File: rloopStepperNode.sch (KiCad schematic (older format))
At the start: 0 parts

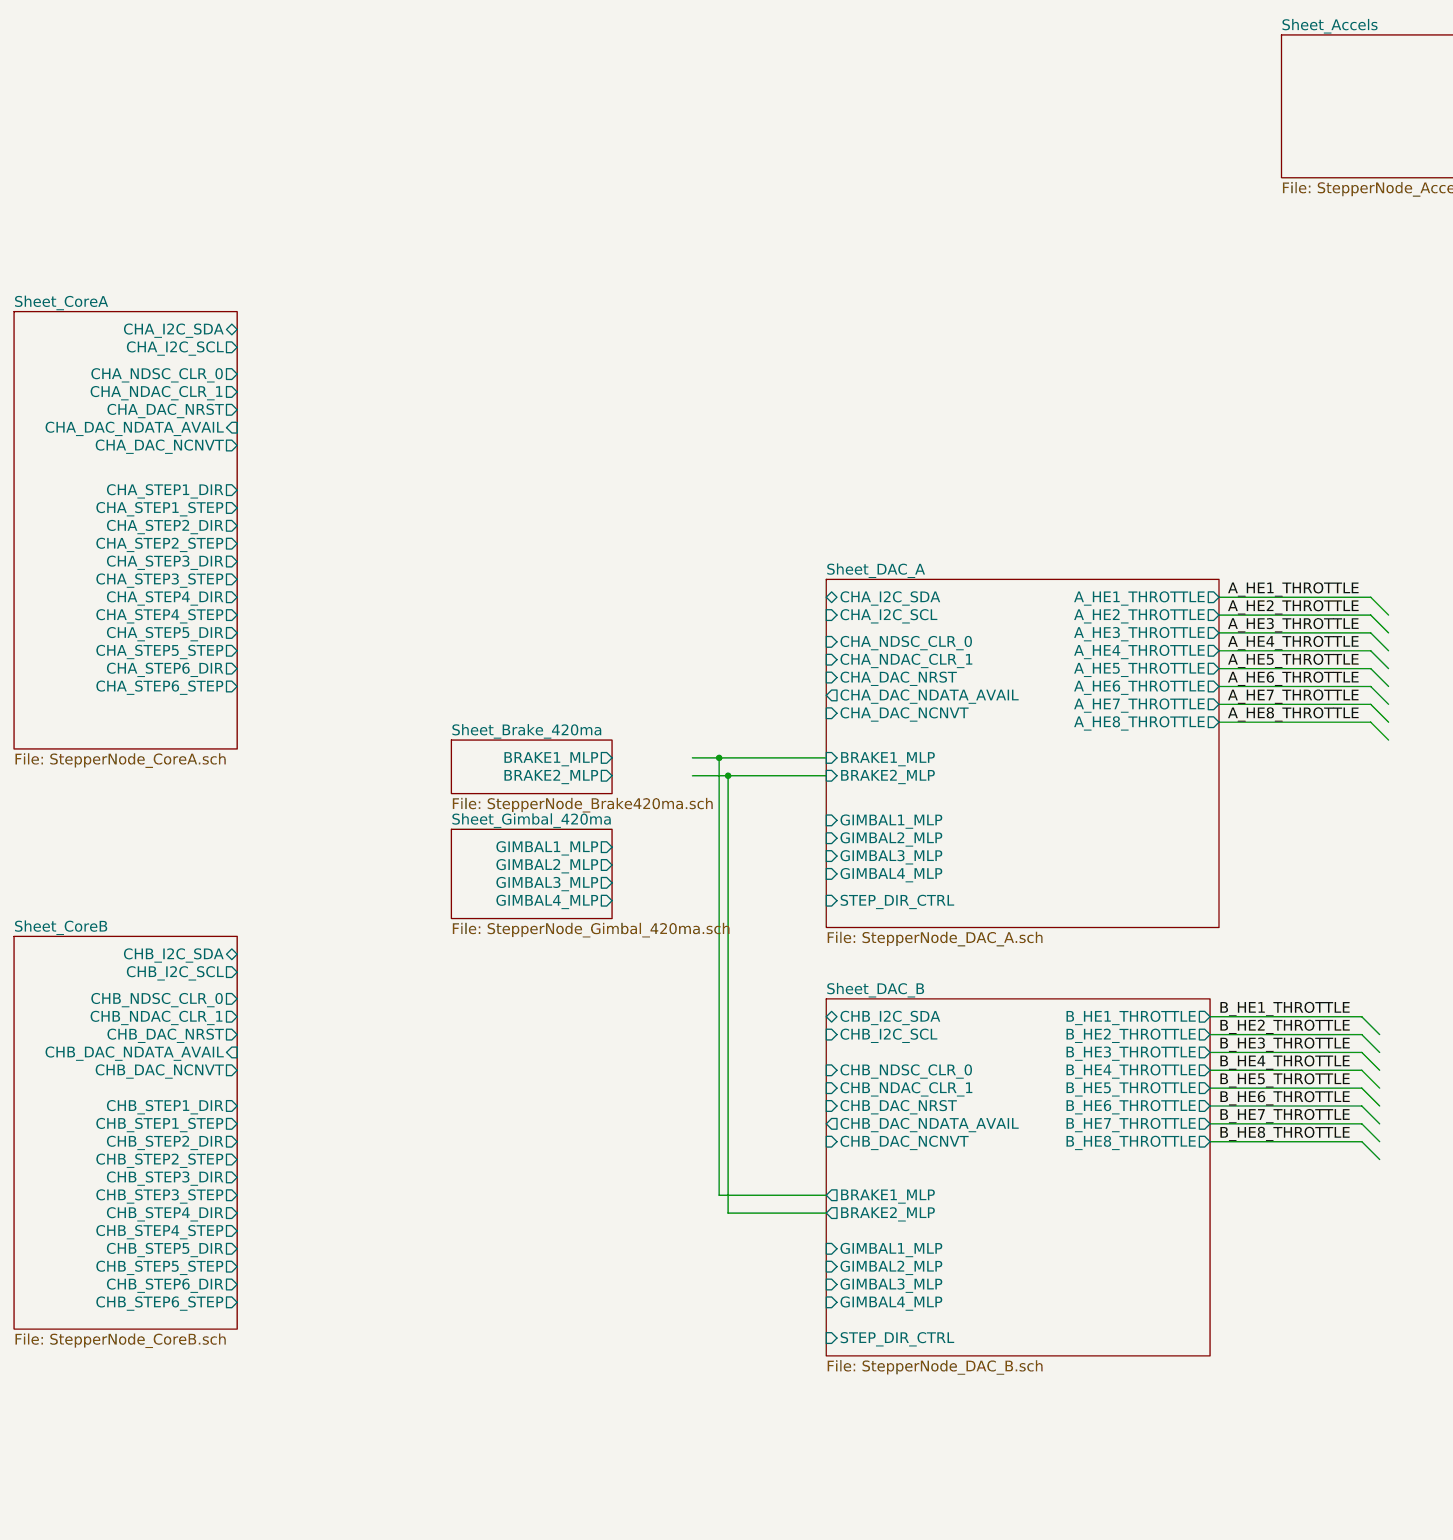
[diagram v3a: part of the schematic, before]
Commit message: Setup Watchdog Sheet
Watchdog is for Channel A/B priority determination.
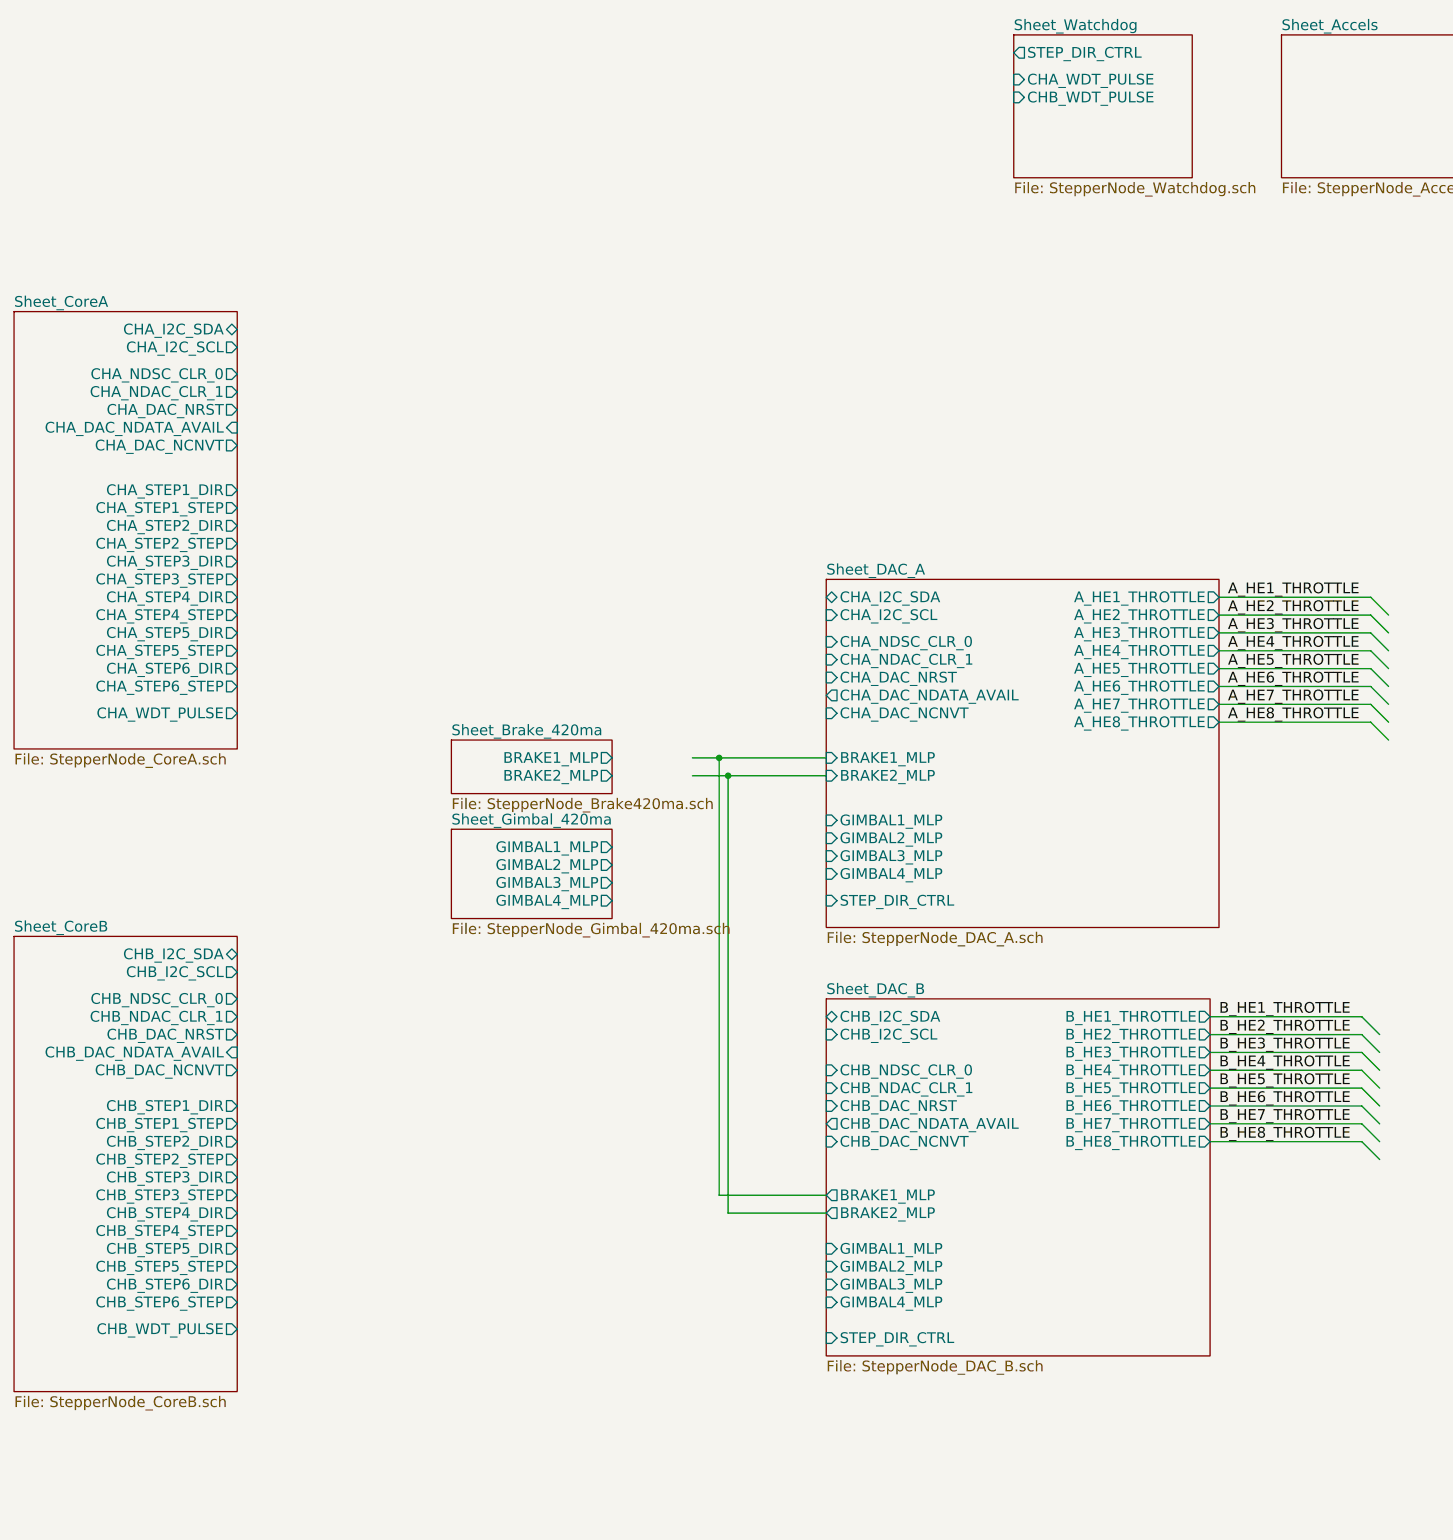
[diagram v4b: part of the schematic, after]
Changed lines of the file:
@@
 $Descr A3 16535 11693
 encoding utf-8
-Sheet 1 12
+Sheet 1 13
 Title "Top Level"
 Date ""
@@
 $EndSheet
 $Sheet
-S 2000 5850 1250 2200
+S 2000 5850 1250 2550
 U 57556833
 F0 "Sheet_CoreB" 60
@@
 F19 "CHB_STEP6_DIR" O R 3250 7800 60
 F20 "CHB_STEP6_STEP" O R 3250 7900 60
+F21 "CHB_WDT_PULSE" O R 3250 8050 60
 $EndSheet
 $Sheet
@@
 F19 "CHA_STEP6_DIR" O R 3250 4350 60
 F20 "CHA_STEP6_STEP" O R 3250 4450 60
+F21 "CHA_WDT_PULSE" O R 3250 4600 60
 $EndSheet
 $Sheet
@@
 F1 "StepperNode_Accels.sch" 60
 $EndSheet
+$Sheet
+S 7600 800  1000 800
+U 5753CE47
+F0 "Sheet_Watchdog" 60
+F1 "StepperNode_Watchdog.sch" 60
+F2 "STEP_DIR_CTRL" O L 7600 900 60
+F3 "CHA_WDT_PULSE" I L 7600 1050 60
+F4 "CHB_WDT_PULSE" I L 7600 1150 60
+$EndSheet
 $EndSCHEMATC

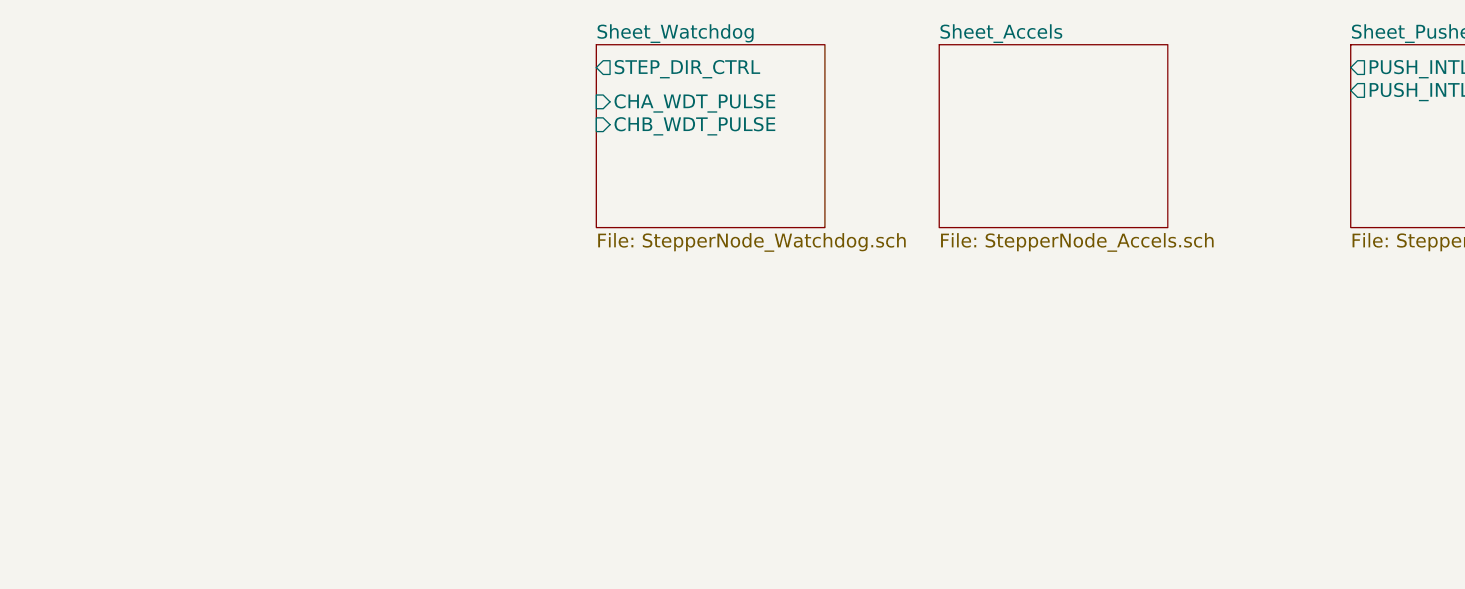
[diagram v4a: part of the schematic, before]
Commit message: Added Brake Failsafe Sheet
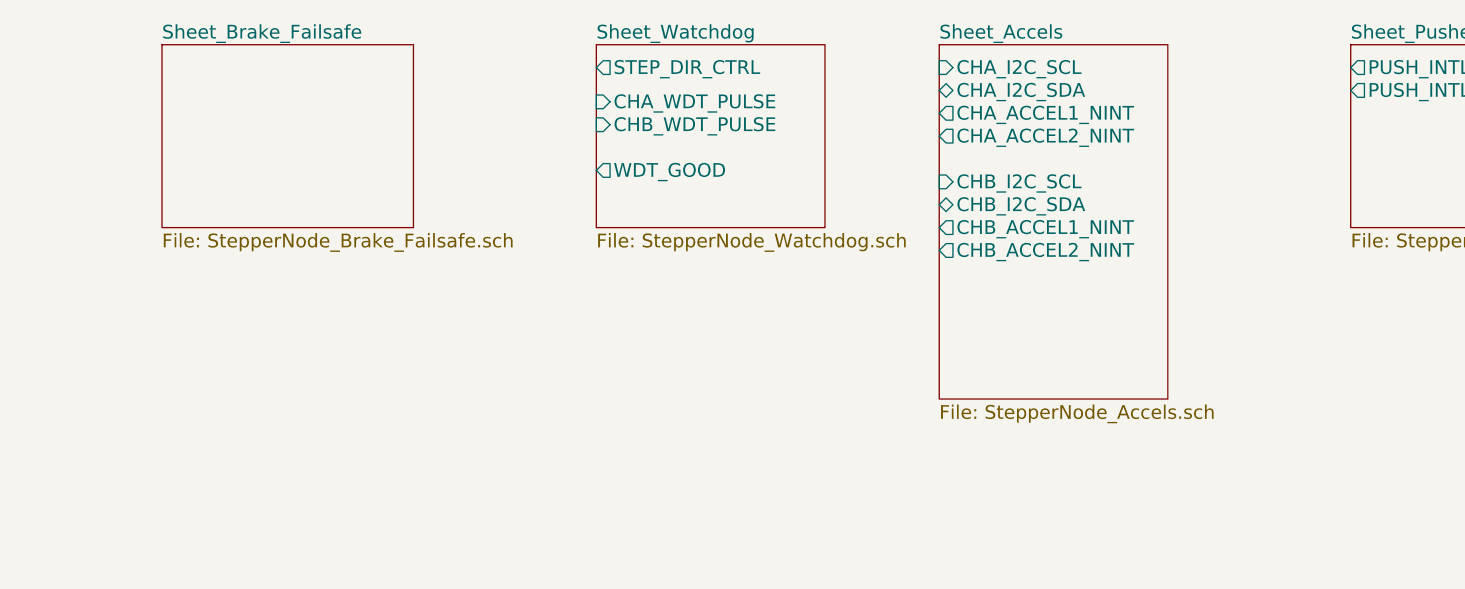
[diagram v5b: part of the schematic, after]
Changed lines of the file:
@@
 $Descr A3 16535 11693
 encoding utf-8
-Sheet 1 13
+Sheet 1 14
 Title "Top Level"
 Date ""
@@
 $EndSheet
 $Sheet
-S 9100 800  1000 800
+S 9100 800  1000 1550
 U 575DC8CA
 F0 "Sheet_Accels" 60
 F1 "StepperNode_Accels.sch" 60
+F2 "CHA_I2C_SCL" I L 9100 900 60
+F3 "CHA_I2C_SDA" B L 9100 1000 60
+F4 "CHA_ACCEL1_NINT" O L 9100 1100 60
+F5 "CHA_ACCEL2_NINT" O L 9100 1200 60
+F6 "CHB_ACCEL1_NINT" O L 9100 1600 60
+F7 "CHB_ACCEL2_NINT" O L 9100 1700 60
+F8 "CHB_I2C_SCL" I L 9100 1400 60
+F9 "CHB_I2C_SDA" B L 9100 1500 60
 $EndSheet
 $Sheet
@@
 F3 "CHA_WDT_PULSE" I L 7600 1050 60
 F4 "CHB_WDT_PULSE" I L 7600 1150 60
+F5 "WDT_GOOD" O L 7600 1350 60
+$EndSheet
+$Sheet
+S 5700 800  1100 800
+U 5754F696
+F0 "Sheet_Brake_Failsafe" 60
+F1 "StepperNode_Brake_Failsafe.sch" 60
 $EndSheet
 $EndSCHEMATC
